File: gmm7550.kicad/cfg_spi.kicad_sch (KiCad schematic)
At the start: 53 parts, among them U1 CCGM1A1, U10 PCA9539AHF, U4 STG3692, U5 STG3692, U6 74LVC1G08, U7 74LVC1G07, U8 STG3692, U9 IS25LQ032B-JNLE

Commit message: Change U7 footprint due to the part availability, revision and date are updated, DRC warnings clean-up (GMM-7550)
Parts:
- U7: footprint Package_TO_SOT_SMD:SOT-353_SC-70-5 -> Package_TO_SOT_SMD:SOT-23-5

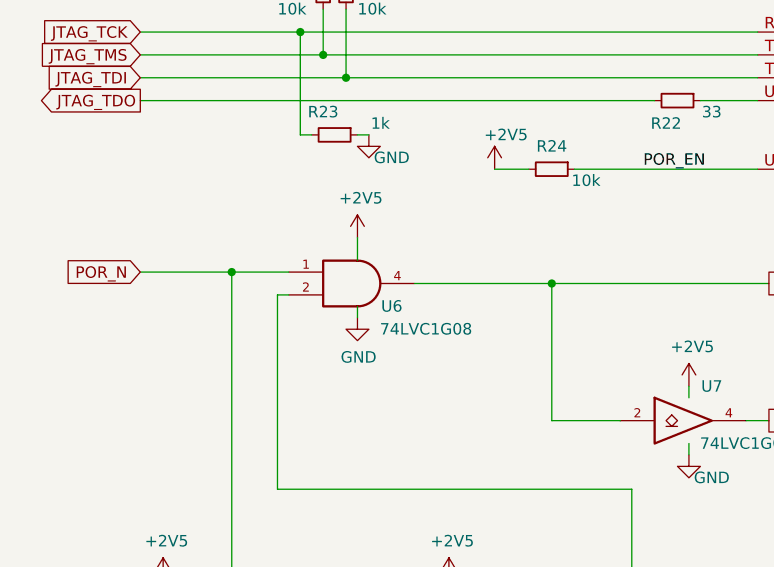
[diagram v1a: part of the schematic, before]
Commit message: Update designs to KiCad v7
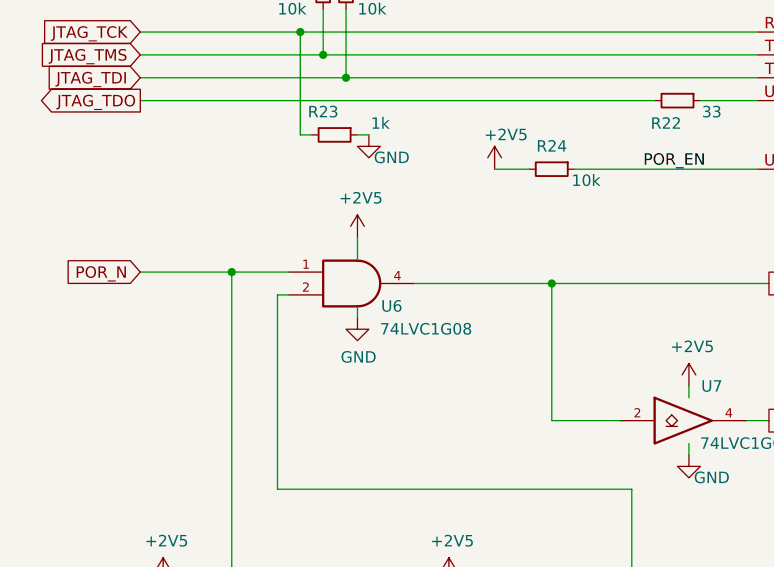
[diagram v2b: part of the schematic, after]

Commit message: Update copyright years and increment revision
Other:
- note added: "Copyright (c) 2020-2024 Anton Kuzmin Licensed under CERN-OHL-P v2 https://github.com/gmm-7550/"
- note removed: "Copyright (c) 2020-2022 Anton Kuzmin Licensed under CERN-OHL-P v2 https://github.com/ak-fau/gmm7550.git"
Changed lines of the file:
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@@
   (title_block
     (title "GateMate FPGA Module: GMM-7550")
-    (date "2022-04-24")
-    (rev "2.1")
+    (date "2022-04-27")
+    (rev "2.2")
   )
   (junction (at 251.46 114.3) (diameter 0) (color 0 0 0 0)
@@
     (stroke (width 0) (type default))
   )
-  (text "Copyright (c) 2020-2022  Anton Kuzmin\nLicensed under CERN-OHL-P v2\nhttps://github.com/ak-fau/gmm7550.git"
+  (text "Copyright (c) 2020-2024  Anton Kuzmin\nLicensed under CERN-OHL-P v2\nhttps://github.com/gmm-7550/"
     (at 198.12 179.07 0)
     (effects (font (size 2.54 2.54)) (justify left bottom))
